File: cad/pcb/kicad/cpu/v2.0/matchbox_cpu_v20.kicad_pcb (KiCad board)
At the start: 6 copper layers, 40 x 66 mm, 68 parts, among them CN1 ?M02B-SRSS-TBS, P1 DF12-32-DP, P2 DF12-32-DP, P3 DF12-32-DP, P4 DF12-32-DP, Q1 FDN360P, Q2 FDN360P, SW1 B3U-3100PM-B, SW2 B3U-3100PM-B, U1 STM32H743VG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

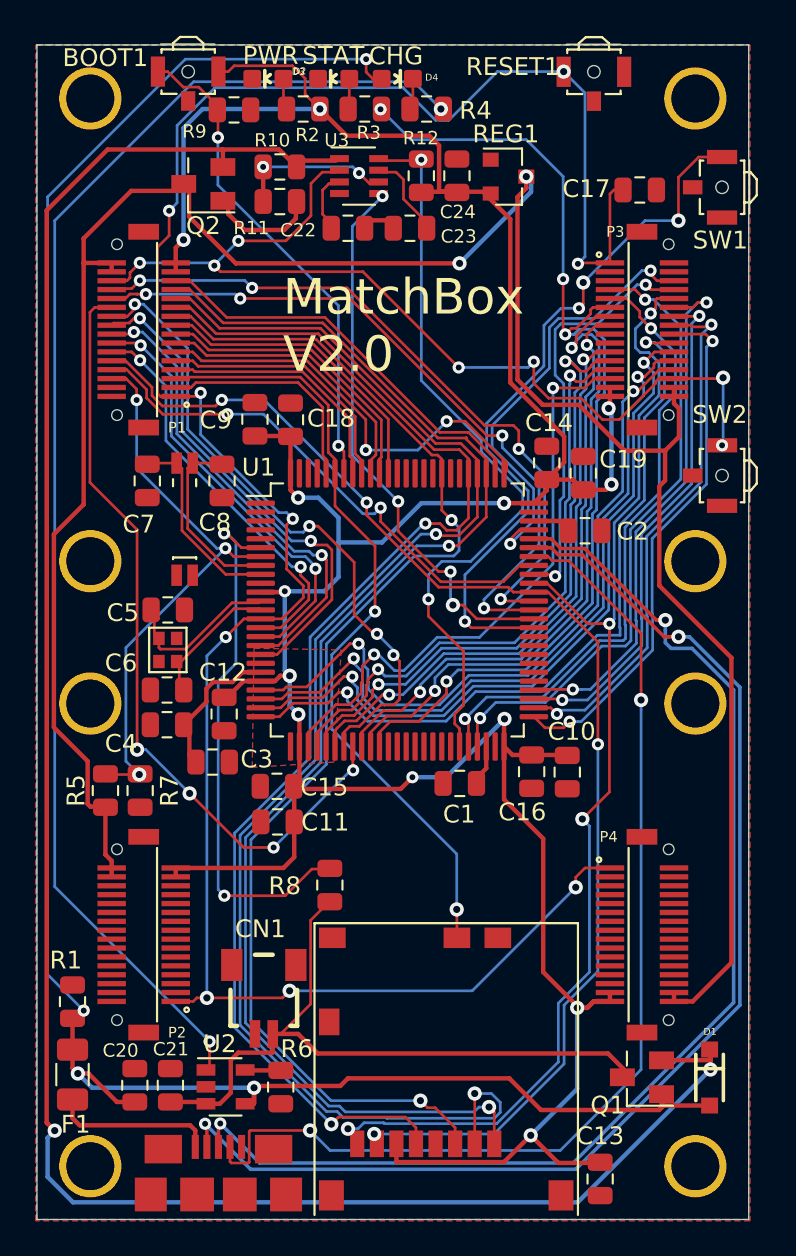
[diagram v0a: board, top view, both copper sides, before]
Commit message: Add 3d models to project
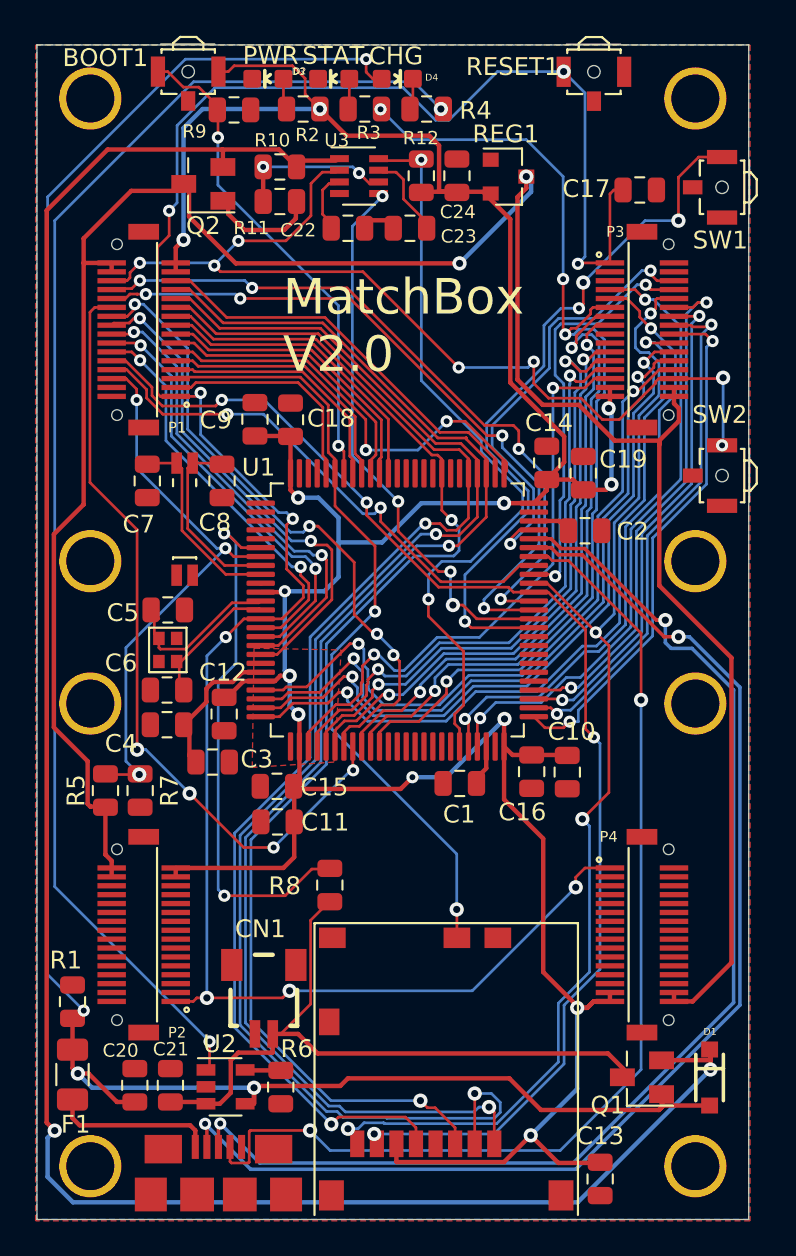
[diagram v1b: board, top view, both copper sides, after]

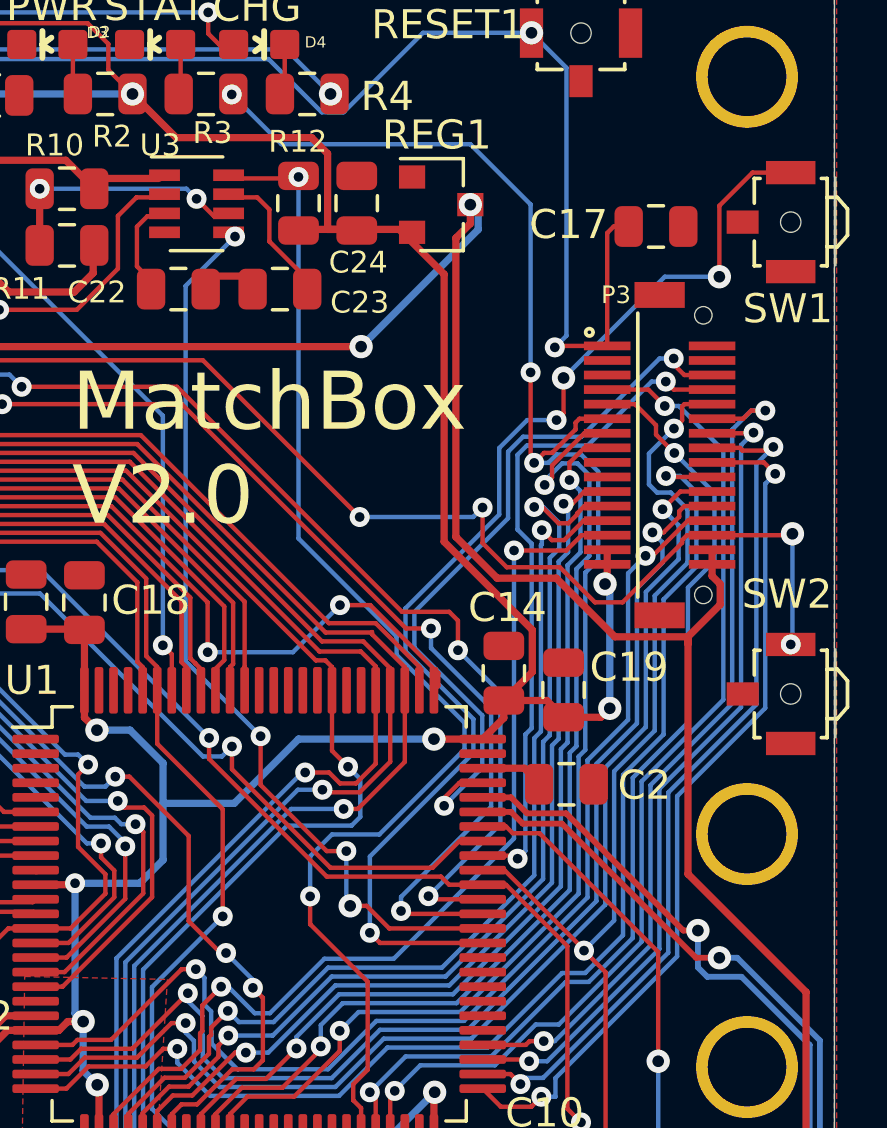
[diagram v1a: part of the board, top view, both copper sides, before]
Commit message: Bypass cap improvements for STM32 part
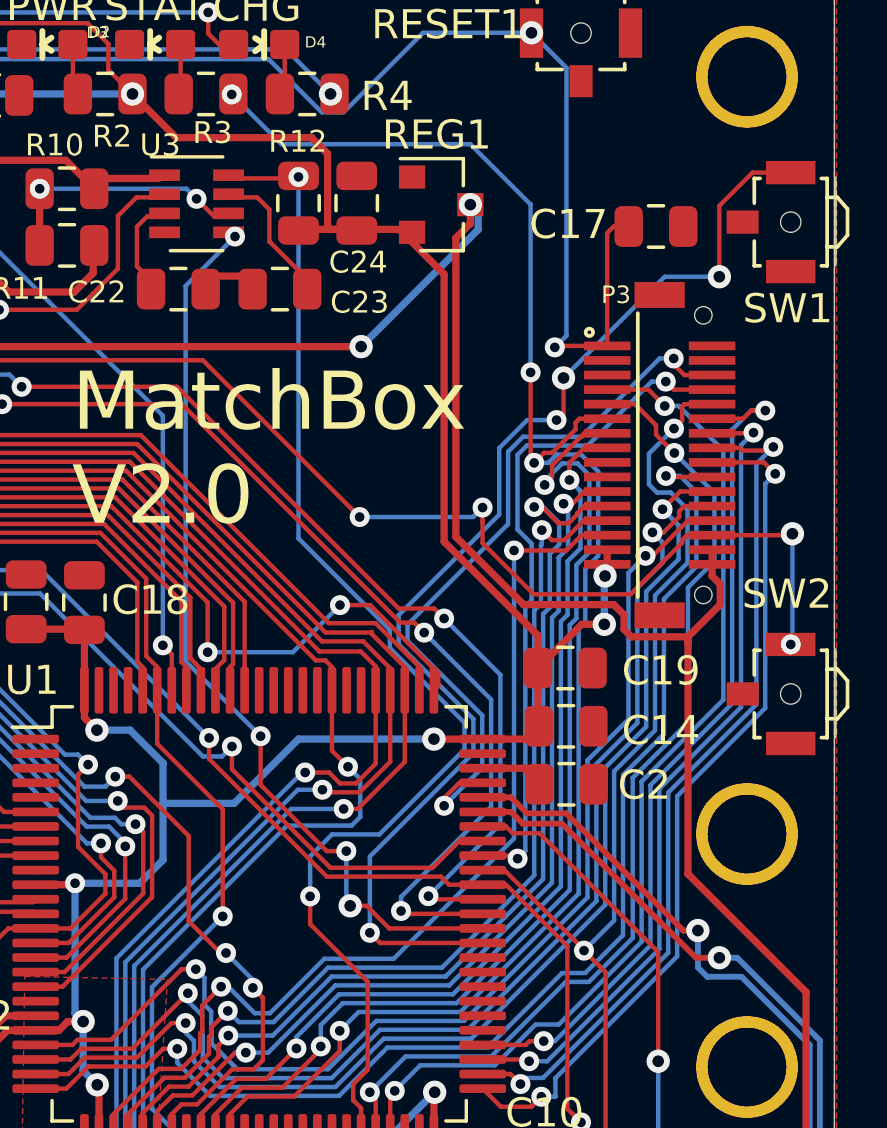
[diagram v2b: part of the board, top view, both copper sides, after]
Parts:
- moved C14 2.81 mm to (30.8, -40.7), turned to 0 degrees
- moved C19 0.76 mm to (30.8, -42.7), turned to 0 degrees
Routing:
- net /VCC_3V3: track 185.6 -> 182.6 mm

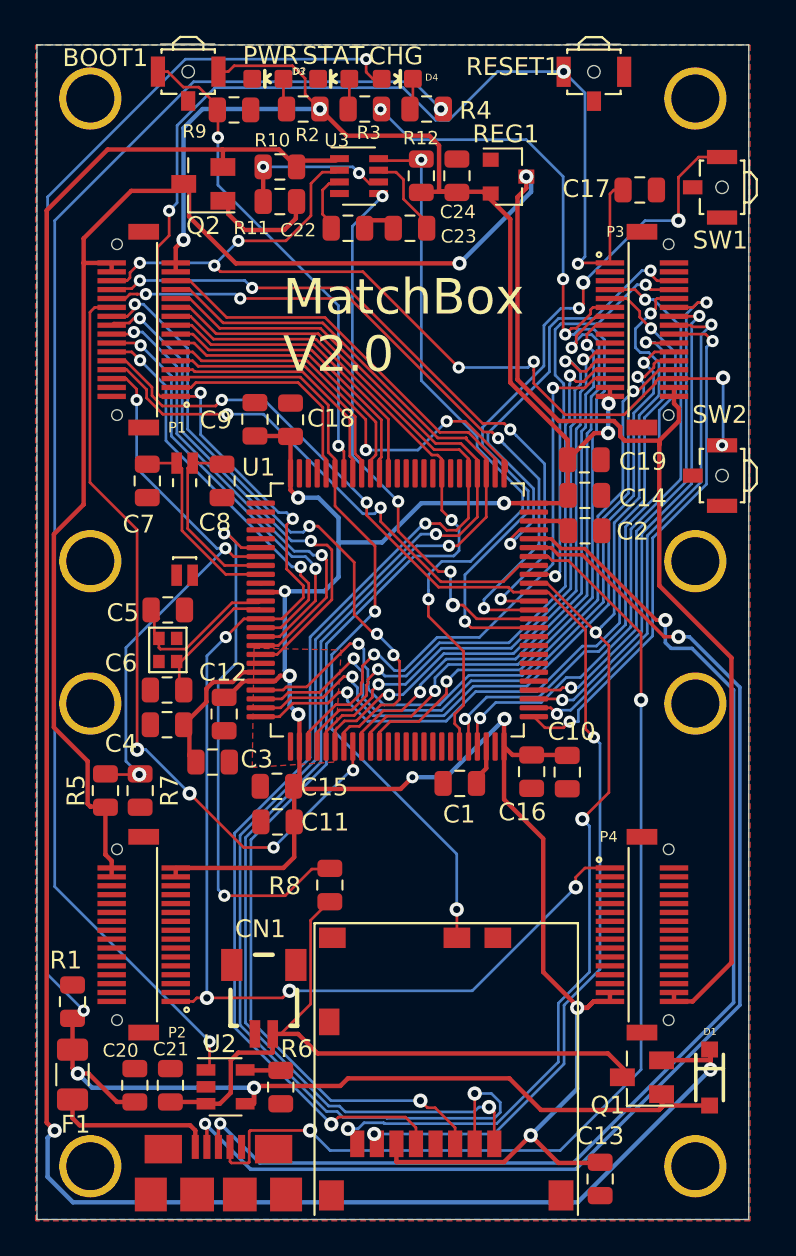
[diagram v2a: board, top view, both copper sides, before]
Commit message: Minor ground plane improvements
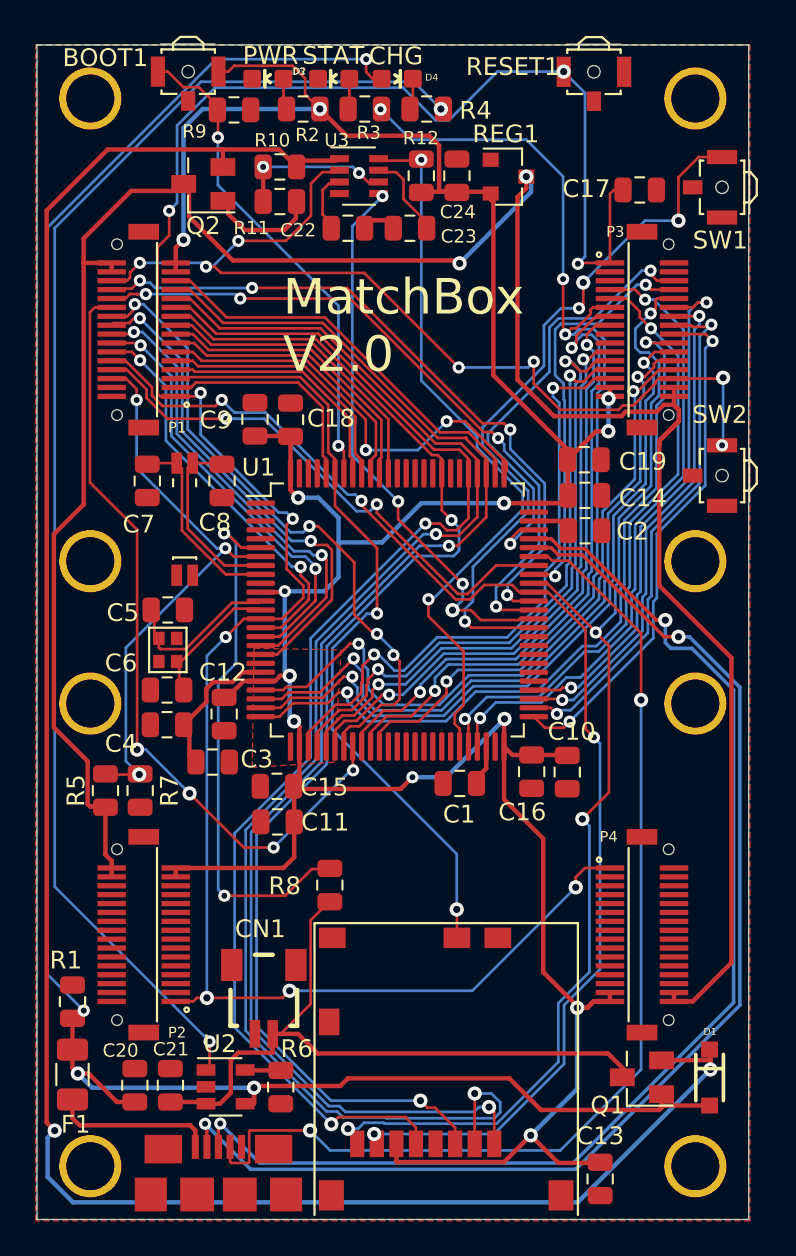
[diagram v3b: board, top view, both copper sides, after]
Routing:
- net /VCC: track 133.4 -> 135.6 mm
- net /PA4: track 33.4 -> 34.6 mm
- net /PC6: track 39.8 -> 38.8 mm
- net /VCC_USBF: track 117.0 -> 116.0 mm
- net /PE15: track 42.0 -> 41.2 mm
- net /PC7: track 39.3 -> 38.7 mm

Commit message: Fix all DRC errors with undefined courtyards
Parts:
- moved R9 0.41 mm to (11.1, -62.0)
- moved D2 0.09 mm to (13.0, -64.2)
- moved D3 0.09 mm to (16.7, -64.2)
- moved D4 0.09 mm to (20.2, -64.2)
- renumbered CN1 to BATT
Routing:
- net /VCC_3V3: track 182.5 -> 183.2 mm
